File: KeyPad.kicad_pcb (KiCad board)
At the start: 2 copper layers, 41.9 x 41.9 mm, 16 parts, among them P1 CONN_01X03, SW1 SW_Push_Dual, SW2 SW_Push_Dual, SW3 SW_Push_Dual, SW4 SW_Push_Dual

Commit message: Logo cambiado
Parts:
- removed the G*** at (154.3, 101.6)
- added G***: LOGO, Grape:atom_medium, B.Cu at (154.3, 102.3)

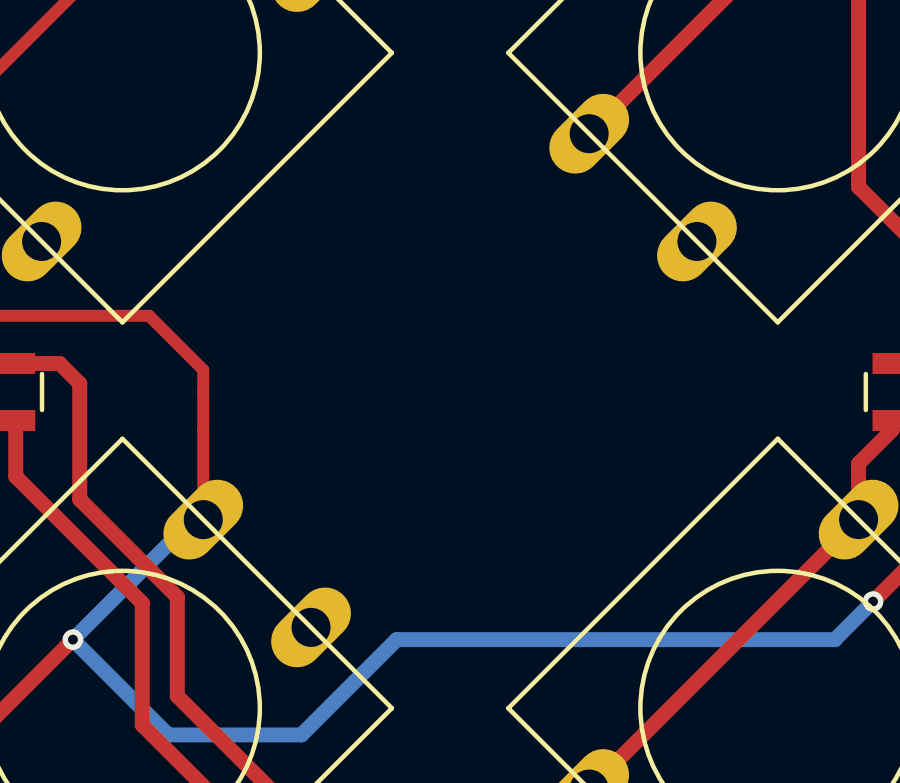
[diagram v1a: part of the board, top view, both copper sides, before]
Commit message: Logos cambiados
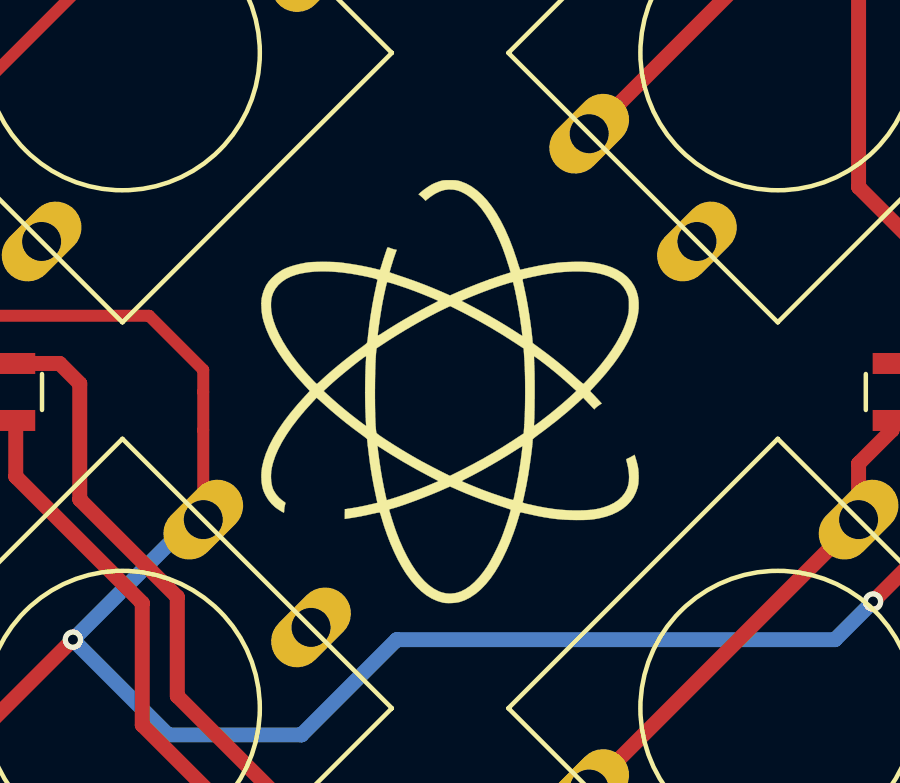
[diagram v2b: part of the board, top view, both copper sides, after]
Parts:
- removed the G*** at (154.3, 102.2)
- removed the G*** at (154.3, 102.3)
- added G***: LOGO, logos_frizzy:atom_XL, F.Cu at (154.2, 102.2)
